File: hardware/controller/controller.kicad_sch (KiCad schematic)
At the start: 34 parts, among them J1 Screw_Terminal_01x02, J2 Screw_Terminal_01x02, J3 Screw_Terminal_01x02, J4 GROVE-CONNECTOR-DIP-90D_4P-2.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, J5 Screw_Terminal_01x03, T1 NMOSFETSOT23, T2 NMOSFETSOT23, T3 NMOSFETSOT23, T4 NMOSFETTO252, T5 NMOSFETTO252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

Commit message: Last version of controller
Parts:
- removed J3: Screw_Terminal_01x02, TerminalBlock_Phoenix:TerminalBlock_Phoenix_PT-1,5-2-3.5-H_1x02_P3.50mm_Horizontal, symbol Connector:Screw_Terminal_01x02
- removed JP1: SolderJumper_3_Bridged12, Jumper:SolderJumper-3_P1.3mm_Bridged2Bar12_Pad1.0x1.5mm, symbol Jumper:SolderJumper_3_Bridged12
- removed R13, R15: 0, fab:fab-R1206FAB, symbol Device:R_US
- removed R4, R8: 10kΩ, fab:fab-R1206FAB, symbol Device:R_US
- removed T2: NMOSFETSOT23, fab-SOT-23, symbol fab:NMOSFETSOT23
- removed T5: NMOSFETTO252, fab-TO252, symbol fab:NMOSFETTO252
- added C3, C5: 1uF, fab-C1206FAB, symbol fab:CAP-UNPOLARIZEDFAB
- added C4, C6: 4.7uF, fab-C1206FAB, symbol fab:CAP-UNPOLARIZEDFAB
- added JP1: Jumper_3_Bridged12, Jumper:SolderJumper-3_P1.3mm_Bridged12_RoundedPad1.0x1.5mm, symbol Jumper:Jumper_3_Bridged12
- added U3, U4: AP7361C-33E, Package_TO_SOT_SMD:SOT-223-3_TabPin2, symbol Regulator_Linear:AP7361C-33E
- R3: value 10kΩ -> 0
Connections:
- net LIGHTMSFT_2 is gone; now on net LIGHTMSFT: J2.2 (Pin_2), T4.3 (D)
- net 3V3: no longer R3.1
- net GND: now also C3.2, C4.2, C5.2, C6.2, U3.2 (GND), U4.2 (GND)
- net LASERPWM_H: no longer R14.1, R14.2
- net VBAT: now also R14.1, R14.2, JP1.1 (A)
- net at R9.2: now also A1.21 (D9); no longer A1.23 (D11)
- net VBUS: now reaches A1.26 (USB)
- net VBUS: now also JP1.3 (B)
- net LIGHTMSFT_1 renamed LIGHTMSFT
- net LIGHTMSFT_1_L renamed 3V3_REG_1
- net 3V3_REG_1: now also J2.1 (Pin_1); no longer A1.21 (D9)
- net LIGHTMSFT_2_H renamed LIGHTMSFT_H
- net LIGHTMSFT_2_L renamed LIGHTMSFT_L
- net LIGHTMSFT_L: now also A1.23 (D11); no longer A1.20 (D6)
- net VOUT renamed 3V3_REG_2
- net 3V3_REG_2: now also C6.1, U4.3 (VO); no longer J2.1 (Pin_1)
- new net: C4.1, R3.1, U3.3 (VO)
- new net VI: C3.1, C5.1, JP1.2 (C), U3.1 (VI), U4.1 (VI)
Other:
- moved on the sheet: A1, C1, C2, H1, H2, J2, J4, J5, R1, R10, R11, R12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

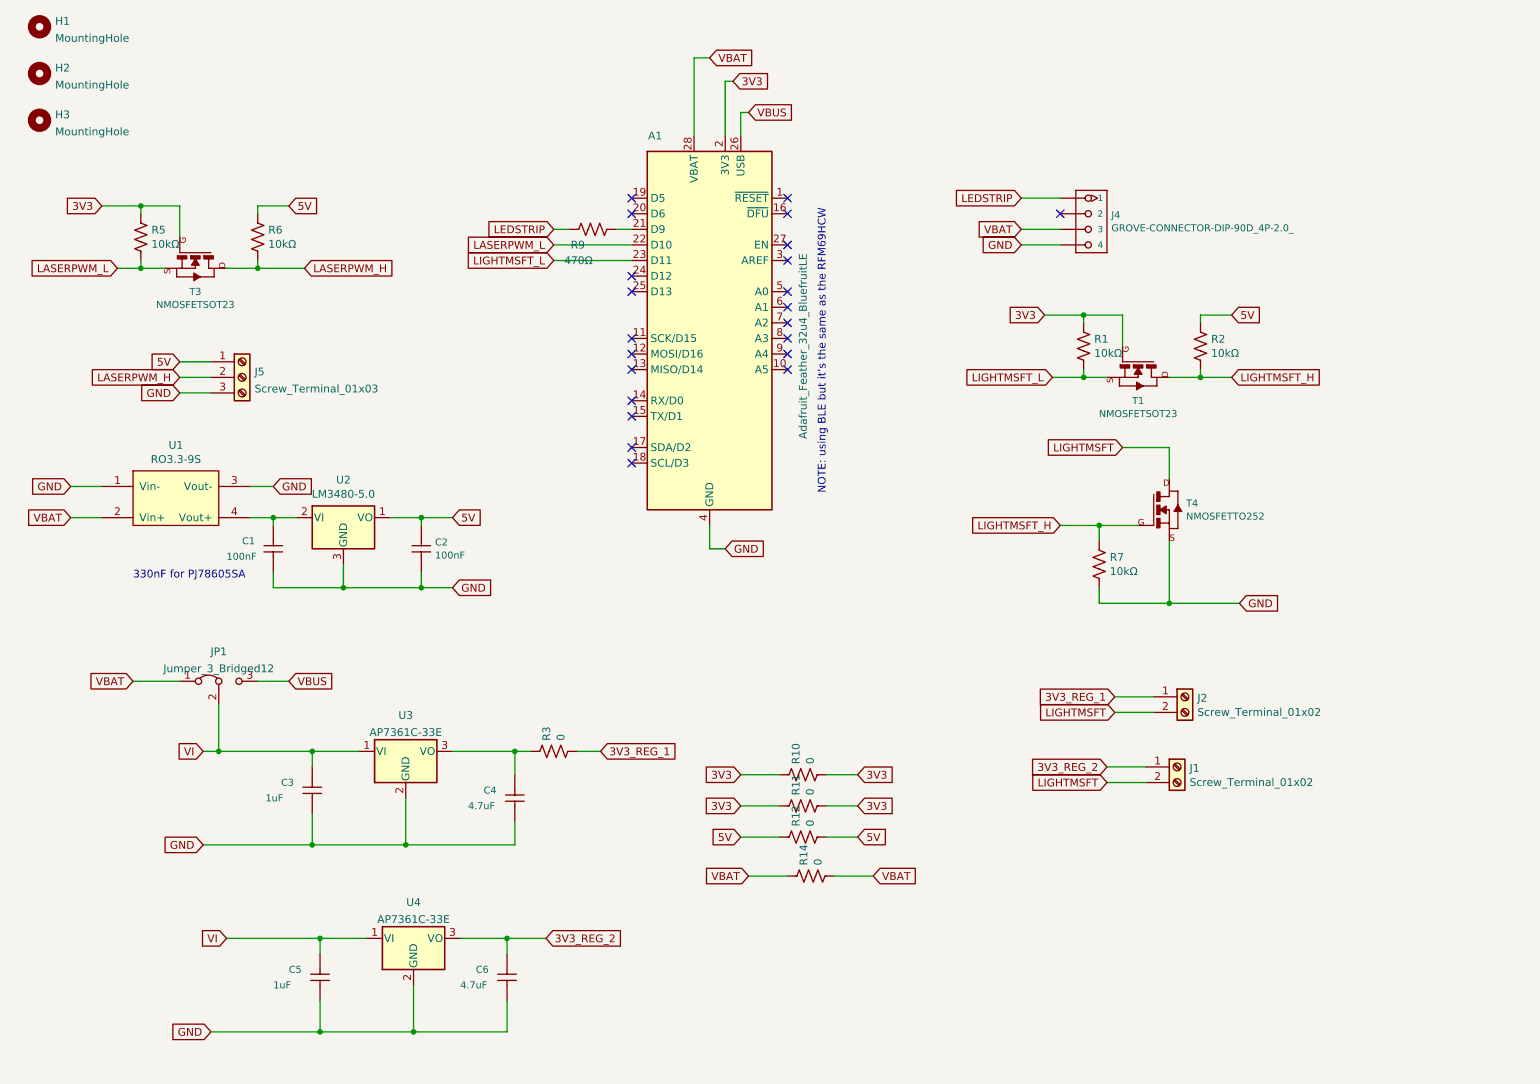
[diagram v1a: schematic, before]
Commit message: electronics with separate power sources and switch
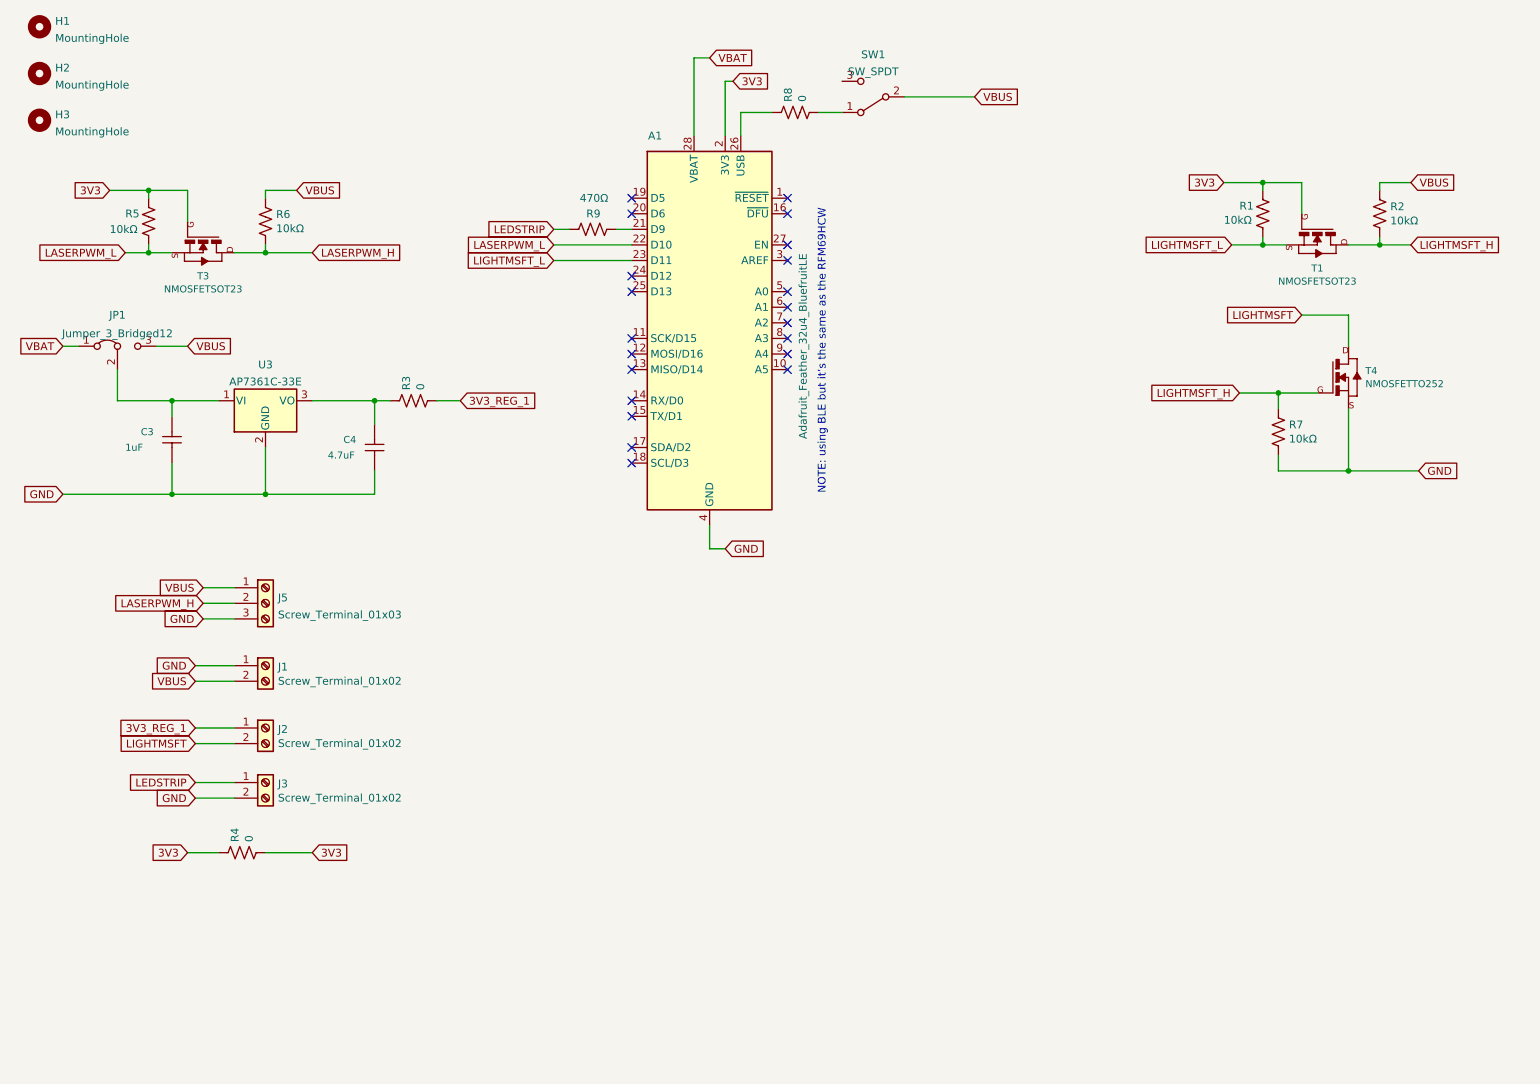
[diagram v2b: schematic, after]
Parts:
- removed C1, C2: 100nF, fab-C1206FAB, symbol fab:CAP-UNPOLARIZEDFAB
- removed C5: 1uF, fab-C1206FAB, symbol fab:CAP-UNPOLARIZEDFAB
- removed C6: 4.7uF, fab-C1206FAB, symbol fab:CAP-UNPOLARIZEDFAB
- removed J4: GROVE-CONNECTOR-DIP-90D_4P-2.0_, OPL_Connector:HW4-2.0-90D, symbol OPL_Connector:GROVE-CONNECTOR-DIP-90D_4P-2.0_
- removed R10, R11, R12, R14: 0, fab:fab-R1206FAB, symbol Device:R_US
- removed U1: RO3.3-9S, Converter_DCDC:Converter_DCDC_RECOM_RO_3.309S, symbol Converter_DCDC:RO3.3-9S
- removed U2: LM3480-5.0, Package_TO_SOT_SMD:SOT-23, symbol Regulator_Linear:LM3480-5.0
- removed U4: AP7361C-33E, Package_TO_SOT_SMD:SOT-223-3_TabPin2, symbol Regulator_Linear:AP7361C-33E
- added J3: Screw_Terminal_01x02, TerminalBlock_Phoenix:TerminalBlock_Phoenix_PT-1,5-2-3.5-H_1x02_P3.50mm_Horizontal, symbol Connector:Screw_Terminal_01x02
- added R4, R8: 0, fab:fab-R1206FAB, symbol Device:R_US
- added SW1: SW_SPDT, fab:fab-SPDTSWITCH, symbol Switch:SW_SPDT
- JP1: footprint Jumper:SolderJumper-3_P1.3mm_Bridged12_RoundedPad1.0x1.5mm -> Jumper:SolderJumper-3_P1.3mm_Bridged12_RoundedPad1.0x1.5mm_NumberLabels
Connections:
- net 3V3_REG_2 is gone; now on net GND: J1.1 (Pin_1)
- net 5V is gone; now on net VBUS: J5.1 (Pin_1), R2.1, R6.1
- net 3V3: now also R4.1, R4.2
- net GND: now also J3.2 (Pin_2)
- net LEDSTRIP: now also J3.1 (Pin_1)
- net LIGHTMSFT: no longer J1.2 (Pin_2)
- net VBUS: now also J1.2 (Pin_2), SW1.2 (B); no longer A1.26 (USB)
- net VI: no longer names the net of C3.1, JP1.2 (C), U3.1 (VI)
- new net: A1.26 (USB), R8.1
- new net: R8.2, SW1.1 (A)
- no-connect marks 22 -> 21
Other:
- note removed: "330nF for PJ78605SA"
- moved on the sheet: C3, C4, J2, J5, R1, R2, R3, R5, R6, R7, T1, T3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
